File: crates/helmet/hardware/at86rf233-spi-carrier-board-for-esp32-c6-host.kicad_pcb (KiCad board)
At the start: 2 copper layers, 30 x 20 mm, 0 parts

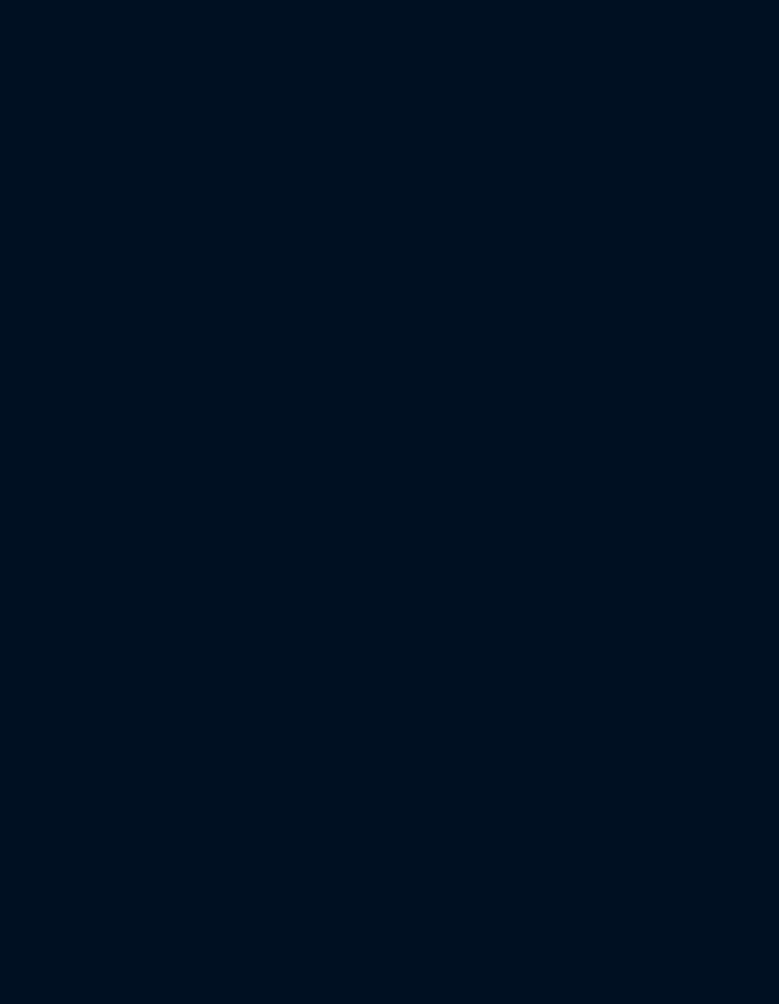
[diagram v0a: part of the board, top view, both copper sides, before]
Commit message: prepare AT86RF233 carrier for PCB layout
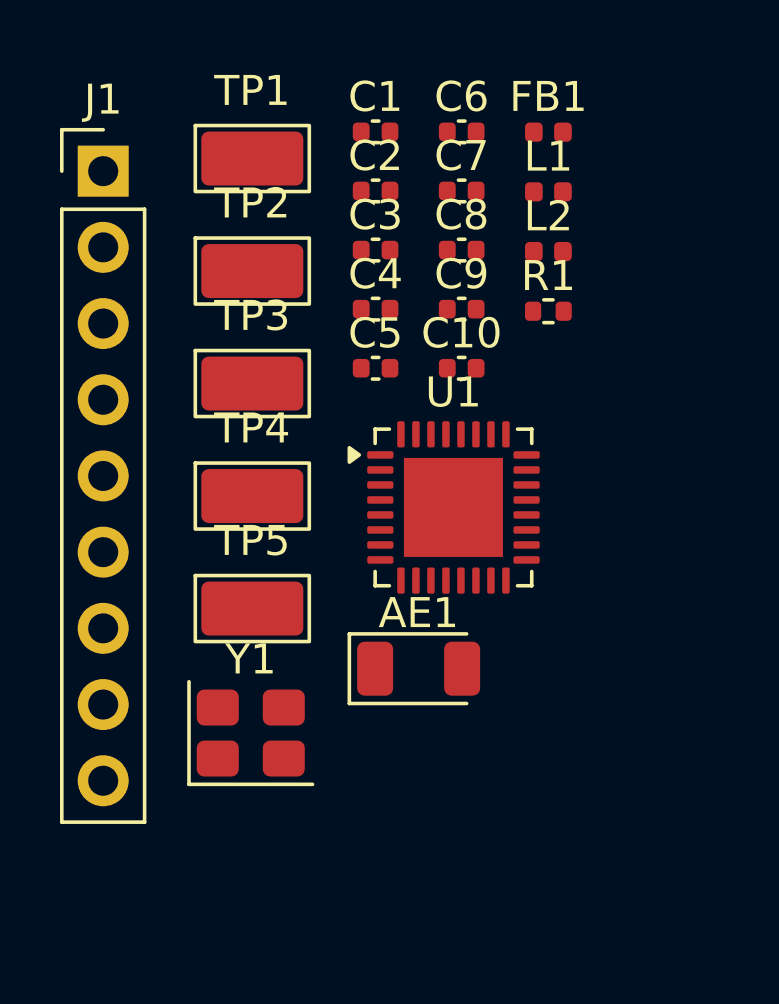
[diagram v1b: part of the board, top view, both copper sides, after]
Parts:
- added AE1: 2.4GHz, RF_Antenna:Johanson_2450AT18x100, F.Cu at (12.3, 18.4)
- added C1: 100nF, Capacitor_SMD:C_0402_1005Metric, F.Cu at (10.9, 0.48)
- added C10: 1.5pF, Capacitor_SMD:C_0402_1005Metric, F.Cu at (13.7, 8.37)
- added C2: 100nF, Capacitor_SMD:C_0402_1005Metric, F.Cu at (10.9, 2.46)
- added C3: 100nF, Capacitor_SMD:C_0402_1005Metric, F.Cu at (10.9, 4.42)
- added C4: 1uF, Capacitor_SMD:C_0402_1005Metric, F.Cu at (10.9, 6.39)
- added C5: 1uF, Capacitor_SMD:C_0402_1005Metric, F.Cu at (10.9, 8.37)
- added C6: 1uF, Capacitor_SMD:C_0402_1005Metric, F.Cu at (13.7, 0.48)
- added C7: 12pF, Capacitor_SMD:C_0402_1005Metric, F.Cu at (13.7, 2.46)
- added C8: 12pF, Capacitor_SMD:C_0402_1005Metric, F.Cu at (13.7, 4.42)
- added C9: 1pF, Capacitor_SMD:C_0402_1005Metric, F.Cu at (13.7, 6.39)
- added FB1: 600R, Inductor_SMD:L_0402_1005Metric, F.Cu at (16.6, 0.49)
- added J1: Conn_01x09, Connector_PinHeader_2.54mm:PinHeader_1x09_P2.54mm_Vertical, F.Cu at (1.79, 1.79)
- added L1: 3.9nH, Inductor_SMD:L_0402_1005Metric, F.Cu at (16.6, 2.48)
- added L2: 3.9nH, Inductor_SMD:L_0402_1005Metric, F.Cu at (16.6, 4.47)
- added R1: 100k, Resistor_SMD:R_0402_1005Metric, F.Cu at (16.6, 6.46)
- added TP1: TestPoint, TestPoint:TestPoint_Keystone_5015_Micro_Mini, F.Cu at (6.76, 1.38)
- added TP2: TestPoint, TestPoint:TestPoint_Keystone_5015_Micro_Mini, F.Cu at (6.76, 5.12)
- added TP3: TestPoint, TestPoint:TestPoint_Keystone_5015_Micro_Mini, F.Cu at (6.76, 8.88)
- added TP4: TestPoint, TestPoint:TestPoint_Keystone_5015_Micro_Mini, F.Cu at (6.76, 12.6)
- added TP5: TestPoint, TestPoint:TestPoint_Keystone_5015_Micro_Mini, F.Cu at (6.76, 16.4)
- added U1: AT86RF233-ZU, Package_DFN_QFN:QFN-32-1EP_5x5mm_P0.5mm_EP3.3x3.3mm, F.Cu at (13.5, 13.0)
- added Y1: 16MHz, Crystal:Crystal_SMD_Abracon_ABM8G-4Pin_3.2x2.5mm, F.Cu at (6.71, 20.5)

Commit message: fix PCB outline and RF footprint placement
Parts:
- added B1: 2450BM15A0015, ciu:Johanson_2450BM15A0015, F.Cu at (23.0, 13.0)
- added C11: 22pF, Capacitor_SMD:C_0402_1005Metric, F.Cu at (20.0, 12.3)
- added C12: 22pF, Capacitor_SMD:C_0402_1005Metric, F.Cu at (20.0, 14.0)
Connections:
- L1 pad 1: /RFP -> /BALUN_OUT
- U1 pad 5: unconnected-(U1-RFN-Pad5) -> /RFN

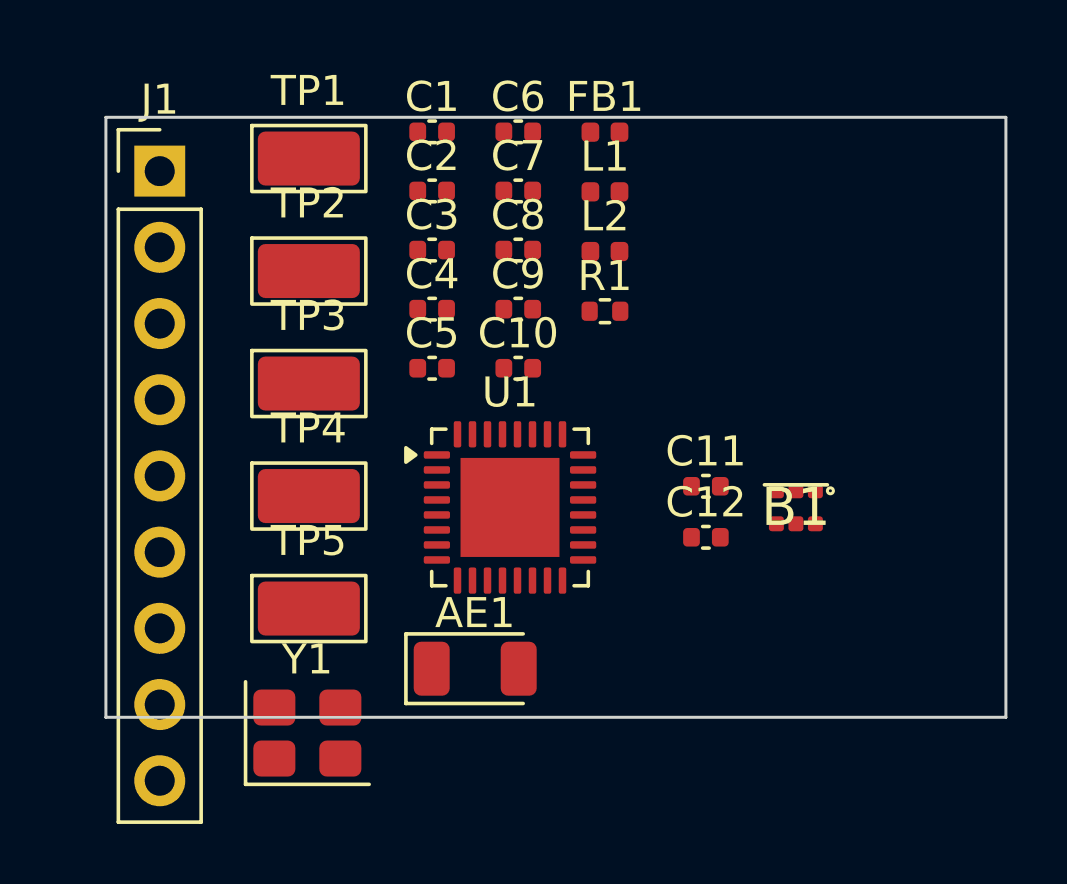
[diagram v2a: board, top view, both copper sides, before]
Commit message: complete PCB placement and routing
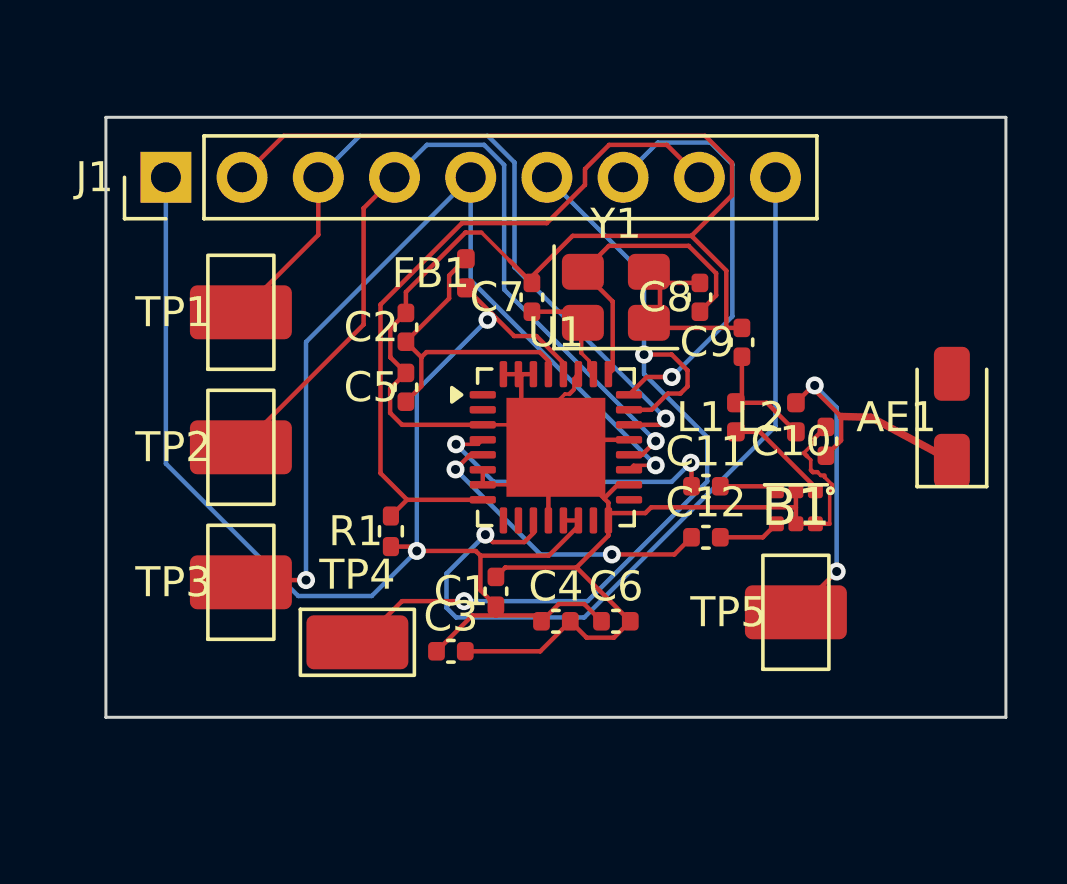
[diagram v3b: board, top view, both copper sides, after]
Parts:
- moved AE1 18.0 mm to (28.2, 10.0), turned to 90 degrees
- moved Y1 17.8 mm to (17.0, 6.00)
- moved C6 16.6 mm to (17.0, 16.8)
- moved TP5 16.2 mm to (23.0, 16.5), turned to 90 degrees
- moved C1 15.5 mm to (13.0, 15.8), turned to 90 degrees
- moved C3 13.4 mm to (11.5, 17.8)
- moved C4 11.2 mm to (15.0, 16.8)
- moved C10 10.5 mm to (24.0, 10.8), turned to 90 degrees
- moved R1 10.2 mm to (9.50, 13.8), turned to 90 degrees
- moved L1 8.69 mm to (21.0, 10.0), turned to 90 degrees
- moved L2 8.43 mm to (23.0, 10.0), turned to 90 degrees
- moved C9 7.54 mm to (21.2, 7.50), turned to 90 degrees
- moved TP3 7.00 mm to (4.50, 15.5), turned to 90 degrees
- moved FB1 6.60 mm to (12.0, 5.20), turned to 90 degrees
- moved TP2 6.30 mm to (4.50, 11.0), turned to 90 degrees
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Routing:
- net GND: track 0.00 -> 95.9 mm
- net 3V3: track 0.00 -> 50.2 mm, vias 0 -> 2
- net /SCLK: track 0.00 -> 31.0 mm, vias 0 -> 2
- net /SEL: track 0.00 -> 30.6 mm, vias 0 -> 2
- net /MISO: track 0.00 -> 27.9 mm, vias 0 -> 1
- net /SLP_TR: track 0.00 -> 27.3 mm, vias 0 -> 1
- net /MOSI: track 0.00 -> 25.0 mm, vias 0 -> 1
- net /RESET: track 0.00 -> 23.7 mm
- net /RF_FEED: track 0.00 -> 16.3 mm, vias 0 -> 2
- net /IRQ: track 0.00 -> 14.0 mm, vias 0 -> 1
- net AVDD: track 0.00 -> 10.9 mm
- net /XTAL2: track 0.00 -> 10.6 mm
- net /RFN: track 0.00 -> 10.4 mm, vias 0 -> 2
- net /RFP: track 0.00 -> 10.4 mm, vias 0 -> 2
- net /RF_MATCH: track 0.00 -> 4.02 mm
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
